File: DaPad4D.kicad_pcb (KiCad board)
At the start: 2 copper layers, 99 x 19 mm, 16 parts, among them J1 Conn_01x12, SW1 SW_Push, SW2 SW_Push, SW3 SW_Push, SW4 SW_Push, SW5 Rotary_Encoder_Switch

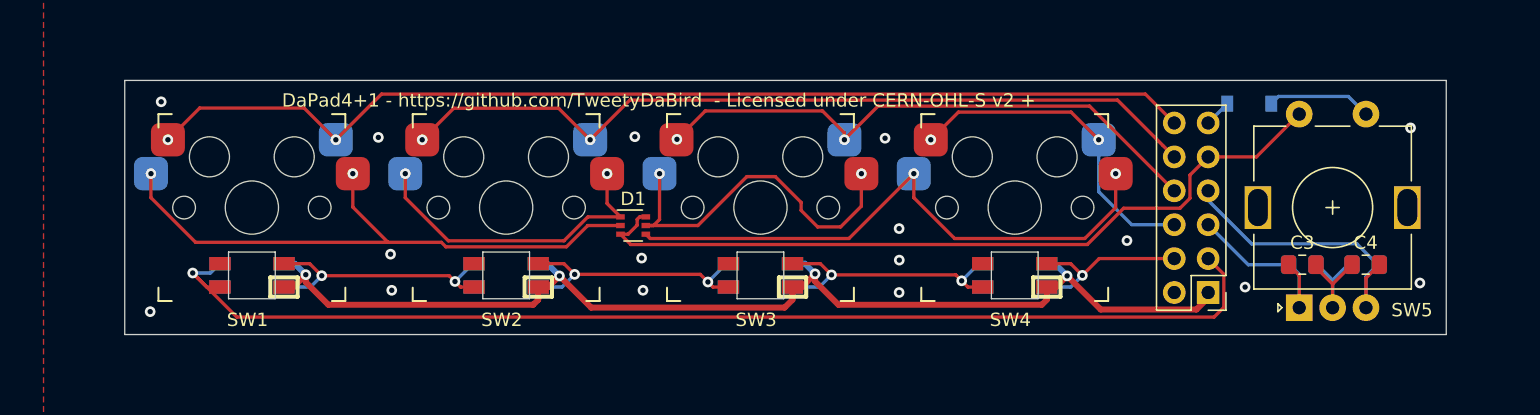
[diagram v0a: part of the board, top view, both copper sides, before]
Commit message: Adjusted dial
Adjusted for more space and larger dialwheel
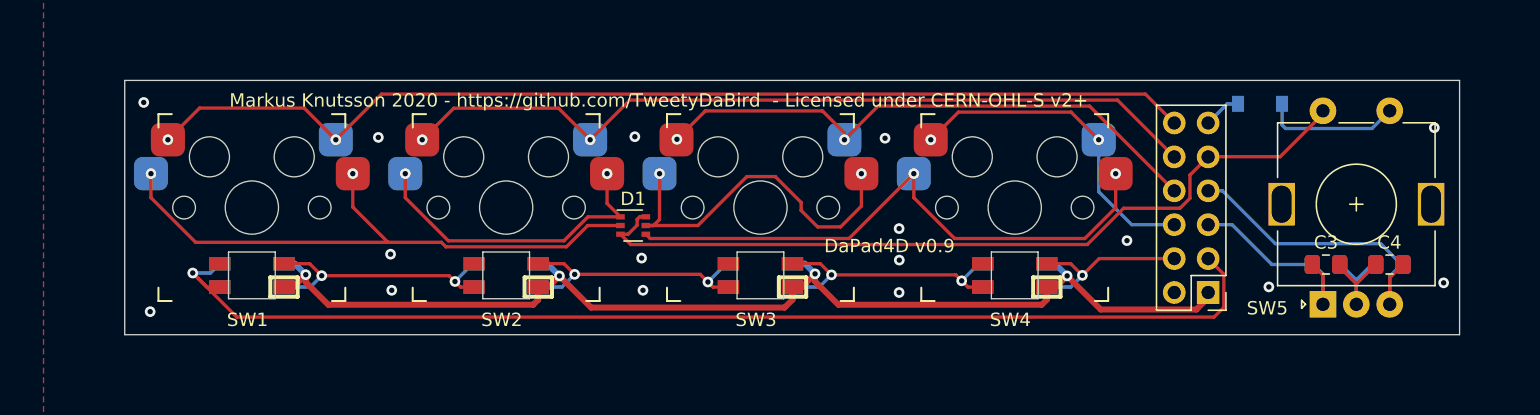
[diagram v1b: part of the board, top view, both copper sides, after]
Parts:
- moved SW5 1.80 mm to (139.5, 60.6)
- moved C1 1.78 mm to (137.2, 65.2)
- moved C2 1.78 mm to (142.0, 65.2)
- moved C3 1.78 mm to (137.2, 65.2)
- moved C4 1.78 mm to (142.0, 65.2)
- moved D2 0.81 mm to (132.3, 53.1)
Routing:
- net Net-(D2-Pad2): track 7.87 -> 10.3 mm
- net D1: track 22.6 -> 24.7 mm
- net Row1: track 58.9 -> 60.7 mm
- net D0: track 14.4 -> 16.2 mm
- net Col5: track 2.04 -> 2.86 mm
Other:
- board size 99 x 19 mm -> 100 x 19 mm
- board text added: "DaPad4D v0.9"
- board text added: "Markus Knutsson 2020 - https://github.com/TweetyDaBird - Licensed under CERN-OHL-S v2+"
- board text removed: "DaPad4+1 - https://github.com/TweetyDaBird - Licensed under CERN-OHL-S v2 +"

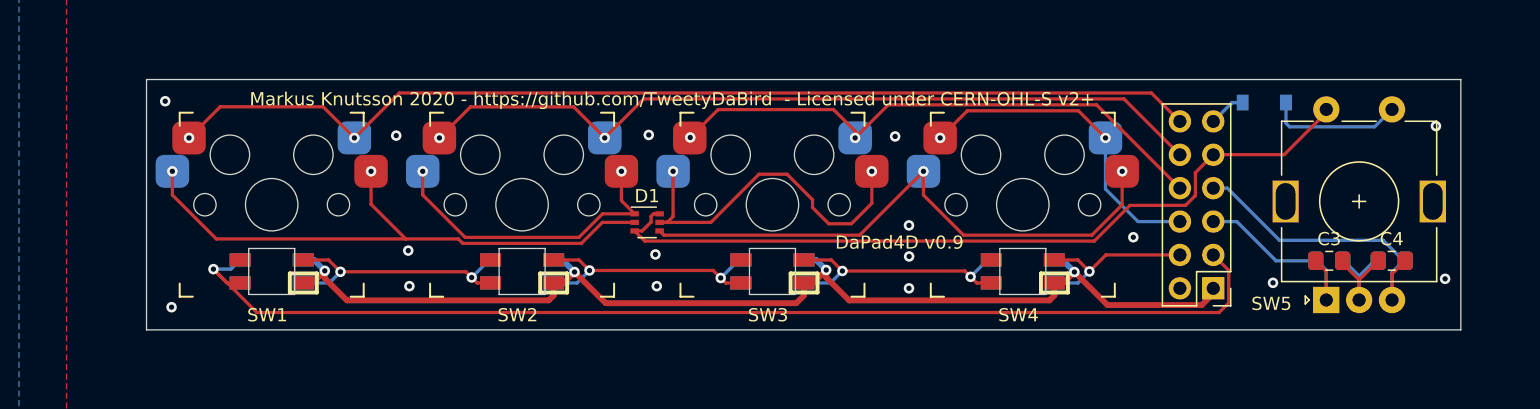
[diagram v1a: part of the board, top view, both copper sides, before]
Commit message: Adjusted for DRC
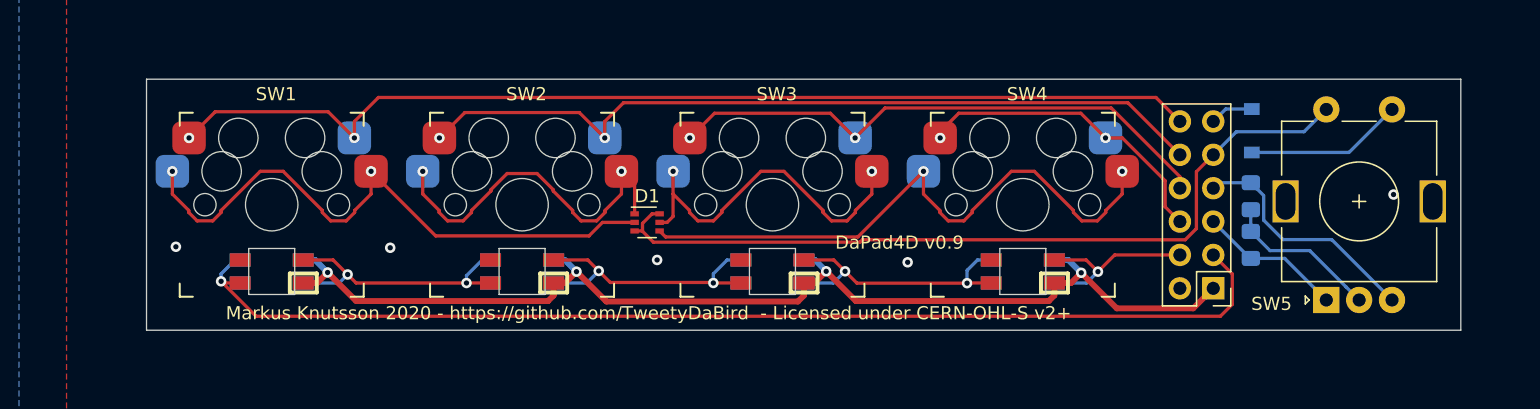
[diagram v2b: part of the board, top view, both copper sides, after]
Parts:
- removed C3, C4: C, Capacitor_SMD:C_0805_2012Metric_Pad1.15x1.40mm_HandSolder
- moved C2 11.8 mm to (131.3, 60.2), turned to 90 degrees
- moved C1 6.09 mm to (131.3, 64.0), turned to 90 degrees
- moved D2 2.35 mm to (131.3, 55.3), turned to 270 degrees
- turned SW1 to 0 degrees
- turned SW2 to 0 degrees
- turned SW3 to 0 degrees
- turned SW4 to 0 degrees
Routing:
- net D1: track 24.7 -> 18.6 mm
- net D0: track 16.2 -> 11.1 mm
- net Net-(D1-Pad1): track 23.7 -> 27.4 mm
- net Net-(D1-Pad4): track 43.9 -> 46.1 mm
- net Net-(D2-Pad2): track 10.3 -> 12.0 mm
- net Net-(D4-Pad1): track 20.5 -> 22.0 mm
- net Net-(D5-Pad1): track 20.1 -> 21.5 mm
- net Net-(D3-Pad1): track 20.4 -> 21.6 mm
- net Row1: track 60.7 -> 61.9 mm
- net RGB_OUT: track 87.8 -> 86.7 mm
- net Col4: track 24.9 -> 23.9 mm
- net Net-(D1-Pad2): track 45.4 -> 46.3 mm
- net Net-(C1-Pad2): track 11.3 -> 12.1 mm
- net RGB_IN: track 13.5 -> 14.1 mm
- net GND: vias 16 -> 5
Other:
- board size 100 x 19 mm -> 100 x 19.1 mm
- net class Default: clearance 0.2 -> 0.15; via_dia 0.8 -> 0.6; via_drill 0.4 -> 0.3
- net class Power: clearance 0.2 -> 0.25
- rule trace_clearance: 0.2 -> 0.15
- rule trace_min: 0.2 -> 0.15
- rule via_min_size: 0.4 -> 0.6
